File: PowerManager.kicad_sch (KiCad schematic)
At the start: 10 parts, among them U2 LM317_SOT-223

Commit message: update goose60 sch footprint
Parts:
- C10, C11, C8, C9: footprint (none) -> Capacitor_SMD:C_0201_0603Metric
- D69: footprint (none) -> Diode_SMD:D_SOD-323F
- R4, R5, R6: footprint (none) -> Resistor_SMD:R_0805_2012Metric
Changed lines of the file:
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@@
       (effects (font (size 1.27 1.27)) (justify left))
     )
-    (property "Footprint" "" (id 2) (at 158.75 116.84 0)
+    (property "Footprint" "Resistor_SMD:R_0805_2012Metric" (id 2) (at 158.75 116.84 0)
       (effects (font (size 1.27 1.27)) hide)
     )
@@
       (effects (font (size 1.27 1.27)) (justify left))
     )
-    (property "Footprint" "" (id 2) (at 129.54 123.19 0)
+    (property "Footprint" "Capacitor_SMD:C_0201_0603Metric" (id 2) (at 129.54 123.19 0)
       (effects (font (size 1.27 1.27)) hide)
     )
@@
       (effects (font (size 1.27 1.27)) (justify left))
     )
-    (property "Footprint" "" (id 2) (at 111.76 123.19 0)
+    (property "Footprint" "Diode_SMD:D_SOD-323F" (id 2) (at 111.76 123.19 0)
       (effects (font (size 1.27 1.27)) hide)
     )
@@
       (effects (font (size 1.27 1.27)) (justify left))
     )
-    (property "Footprint" "" (id 2) (at 204.47 121.92 0)
+    (property "Footprint" "Capacitor_SMD:C_0201_0603Metric" (id 2) (at 204.47 121.92 0)
       (effects (font (size 1.27 1.27)) hide)
     )
@@
       (effects (font (size 1.27 1.27)) (justify left))
     )
-    (property "Footprint" "" (id 2) (at 173.99 129.54 0)
+    (property "Footprint" "Resistor_SMD:R_0805_2012Metric" (id 2) (at 173.99 129.54 0)
       (effects (font (size 1.27 1.27)) hide)
     )
@@
       (effects (font (size 1.27 1.27)) (justify left))
     )
-    (property "Footprint" "" (id 2) (at 187.96 121.92 0)
+    (property "Footprint" "Capacitor_SMD:C_0201_0603Metric" (id 2) (at 187.96 121.92 0)
       (effects (font (size 1.27 1.27)) hide)
     )
@@
       (effects (font (size 1.27 1.27)) (justify left))
     )
-    (property "Footprint" "" (id 2) (at 144.78 129.54 0)
+    (property "Footprint" "Capacitor_SMD:C_0201_0603Metric" (id 2) (at 144.78 129.54 0)
       (effects (font (size 1.27 1.27)) hide)
     )
@@
       (effects (font (size 1.27 1.27)) (justify left))
     )
-    (property "Footprint" "" (id 2) (at 158.75 129.54 0)
+    (property "Footprint" "Resistor_SMD:R_0805_2012Metric" (id 2) (at 158.75 129.54 0)
       (effects (font (size 1.27 1.27)) hide)
     )

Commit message: update components location
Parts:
- C10, C11, C8, C9: footprint Capacitor_SMD:C_0201_0603Metric -> Capacitor_SMD:C_0603_1608Metric
- D69, D70: footprint Diode_SMD:D_SOD-323F -> Diode_SMD:D_0603_1608Metric
- R4, R5, R6: footprint Resistor_SMD:R_0805_2012Metric -> Resistor_SMD:R_0603_1608Metric
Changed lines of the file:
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@@
       (effects (font (size 1.27 1.27)) (justify left))
     )
-    (property "Footprint" "Resistor_SMD:R_0805_2012Metric" (id 2) (at 158.75 116.84 0)
+    (property "Footprint" "Resistor_SMD:R_0603_1608Metric" (id 2) (at 158.75 116.84 0)
       (effects (font (size 1.27 1.27)) hide)
     )
@@
       (effects (font (size 1.27 1.27)) (justify left))
     )
-    (property "Footprint" "Capacitor_SMD:C_0201_0603Metric" (id 2) (at 129.54 123.19 0)
+    (property "Footprint" "Capacitor_SMD:C_0603_1608Metric" (id 2) (at 129.54 123.19 0)
       (effects (font (size 1.27 1.27)) hide)
     )
@@
       (effects (font (size 1.27 1.27)) (justify left))
     )
-    (property "Footprint" "Diode_SMD:D_SOD-323F" (id 2) (at 111.76 123.19 0)
+    (property "Footprint" "Diode_SMD:D_0603_1608Metric" (id 2) (at 111.76 123.19 0)
       (effects (font (size 1.27 1.27)) hide)
     )
@@
       (effects (font (size 1.27 1.27)) (justify left))
     )
-    (property "Footprint" "Capacitor_SMD:C_0201_0603Metric" (id 2) (at 204.47 121.92 0)
+    (property "Footprint" "Capacitor_SMD:C_0603_1608Metric" (id 2) (at 204.47 121.92 0)
       (effects (font (size 1.27 1.27)) hide)
     )
@@
       (effects (font (size 1.27 1.27)) (justify left))
     )
-    (property "Footprint" "Resistor_SMD:R_0805_2012Metric" (id 2) (at 173.99 129.54 0)
+    (property "Footprint" "Resistor_SMD:R_0603_1608Metric" (id 2) (at 173.99 129.54 0)
       (effects (font (size 1.27 1.27)) hide)
     )
@@
       (effects (font (size 1.27 1.27)) (justify left))
     )
-    (property "Footprint" "Capacitor_SMD:C_0201_0603Metric" (id 2) (at 187.96 121.92 0)
+    (property "Footprint" "Capacitor_SMD:C_0603_1608Metric" (id 2) (at 187.96 121.92 0)
       (effects (font (size 1.27 1.27)) hide)
     )
@@
       (effects (font (size 1.27 1.27)) (justify left))
     )
-    (property "Footprint" "Diode_SMD:D_SOD-323F" (id 2) (at 169.545 116.84 0)
+    (property "Footprint" "Diode_SMD:D_0603_1608Metric" (id 2) (at 169.545 116.84 0)
       (effects (font (size 1.27 1.27)) hide)
     )
@@
       (effects (font (size 1.27 1.27)) (justify left))
     )
-    (property "Footprint" "Capacitor_SMD:C_0201_0603Metric" (id 2) (at 144.78 129.54 0)
+    (property "Footprint" "Capacitor_SMD:C_0603_1608Metric" (id 2) (at 144.78 129.54 0)
       (effects (font (size 1.27 1.27)) hide)
     )
@@
       (effects (font (size 1.27 1.27)) (justify left))
     )
-    (property "Footprint" "Resistor_SMD:R_0805_2012Metric" (id 2) (at 158.75 129.54 0)
+    (property "Footprint" "Resistor_SMD:R_0603_1608Metric" (id 2) (at 158.75 129.54 0)
       (effects (font (size 1.27 1.27)) hide)
     )

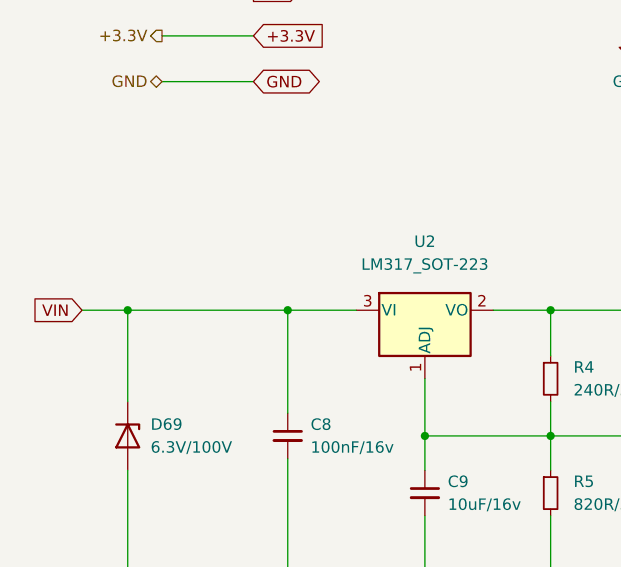
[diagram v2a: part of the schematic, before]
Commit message: add res and fix rule check fail problom
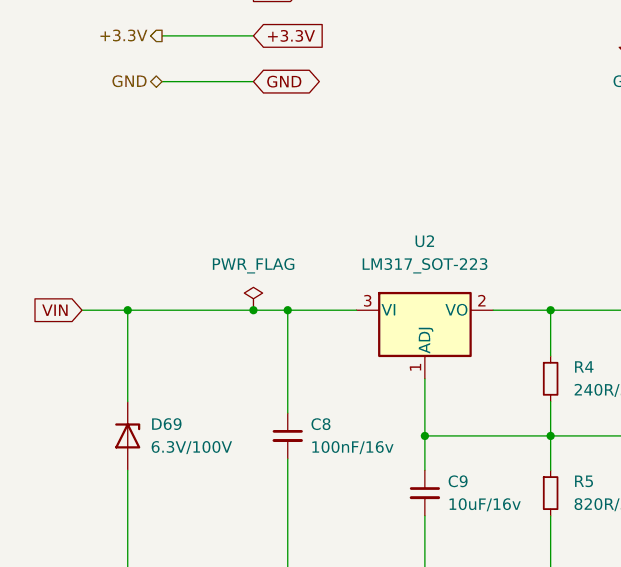
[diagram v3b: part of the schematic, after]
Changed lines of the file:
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@@
   (junction (at 158.75 138.43) (diameter 0) (color 0 0 0 0)
   )
+  (junction (at 125.73 109.22) (diameter 0) (color 0 0 0 0)
+  )
   (junction (at 173.99 123.19) (diameter 0) (color 0 0 0 0)
   )
@@
     (stroke (width 0) (type default) (color 0 0 0 0))
   )
-  (wire (pts (xy 111.76 109.22) (xy 129.54 109.22))
+  (wire (pts (xy 111.76 109.22) (xy 125.73 109.22))
     (stroke (width 0) (type default) (color 0 0 0 0))
   )
@@
   )
   (wire (pts (xy 144.78 138.43) (xy 147.32 138.43))
+    (stroke (width 0) (type default) (color 0 0 0 0))
+  )
+  (wire (pts (xy 125.73 109.22) (xy 129.54 109.22))
     (stroke (width 0) (type default) (color 0 0 0 0))
   )
@@
       (effects (font (size 1.27 1.27)) hide)
     )
+    (pin "1")
+  )
+  (symbol (lib_id "power:PWR_FLAG") (at 125.73 109.22 0) (unit 1)
+    (in_bom yes) (on_board yes) (fields_autoplaced)
+    (property "Reference" "#FLG0101" (id 0) (at 125.73 107.315 0)
+      (effects (font (size 1.27 1.27)) hide)
+    )
+    (property "Value" "PWR_FLAG" (id 1) (at 125.73 104.14 0))
+    (property "Footprint" "" (id 2) (at 125.73 109.22 0)
+      (effects (font (size 1.27 1.27)) hide)
+    )
+    (property "Datasheet" "~" (id 3) (at 125.73 109.22 0)
+      (effects (font (size 1.27 1.27)) hide)
+    )

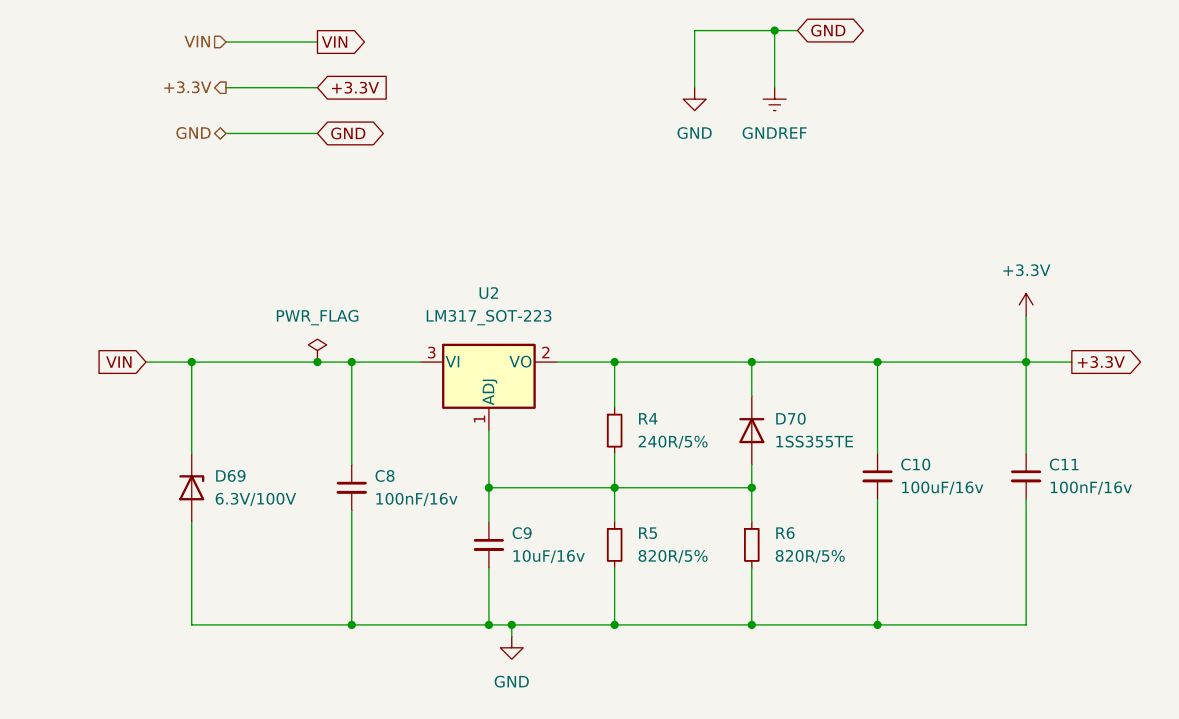
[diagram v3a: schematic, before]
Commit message: modify power/bootload circuit
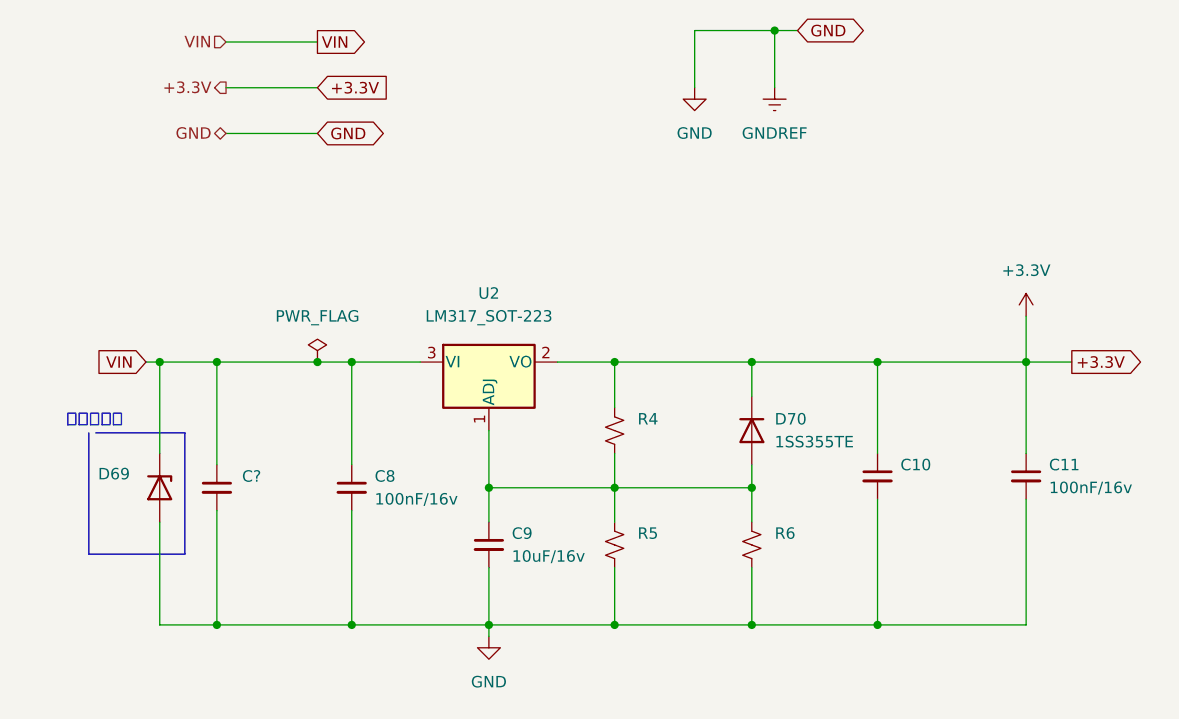
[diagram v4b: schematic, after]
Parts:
- added C?: (no value), symbol Device:C_Small
- C10: value 100uF/16v -> (none); footprint Capacitor_SMD:C_0603_1608Metric -> (none)
- D69: value 6.3V/100V -> (none)
- R4: value 240R/5% -> (none); footprint Resistor_SMD:R_0603_1608Metric -> (none); symbol Device:R_Small -> Device:R_Small_US
- R5, R6: value 820R/5% -> (none); footprint Resistor_SMD:R_0603_1608Metric -> (none); symbol Device:R_Small -> Device:R_Small_US
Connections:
- net GND: now also C?.2
- net VIN: now also C?.1
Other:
- note added: "用途待確認"
- moved on the sheet: D69

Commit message: modify pcb footprint
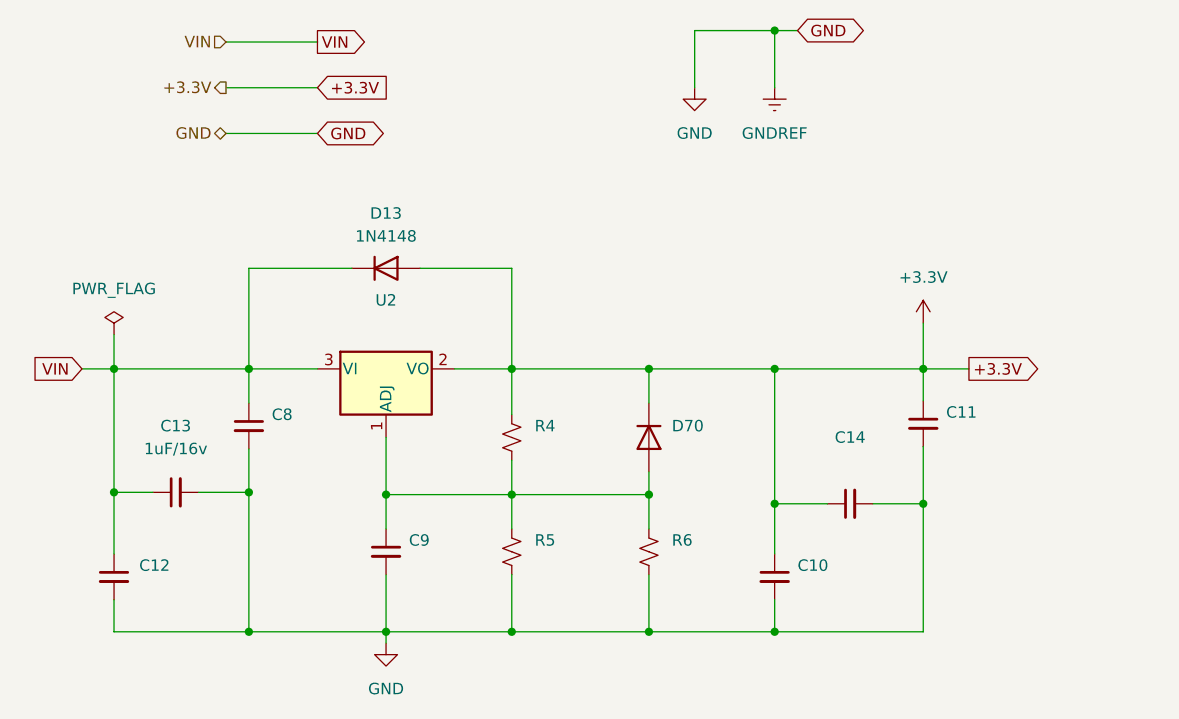
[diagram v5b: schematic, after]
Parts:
- removed D69: (no value), Diode_SMD:D_0603_1608Metric, symbol Device:D_Zener
- added C13: 1uF/16v, Capacitor_SMD:C_0603_1608Metric, symbol Device:C_Small
- added C14: (no value), Capacitor_SMD:C_0603_1608Metric, symbol Device:C_Small
- added D13: 1N4148, Diode_SMD:D_0805_2012Metric, symbol Diode:1SS355VM
- C11, C8: value 100nF/16v -> (none); footprint Capacitor_SMD:C_0603_1608Metric -> (none)
- C9: value 10uF/16v -> (none); footprint Capacitor_SMD:C_0603_1608Metric -> (none)
- D70: value 1SS355TE -> (none); footprint Diode_SMD:D_0603_1608Metric -> (none)
- U2: value LM317_SOT-223 -> (none); footprint Package_TO_SOT_SMD:SOT-223-3_TabPin2 -> (none)
- gave numbers to parts that had none: 1
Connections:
- net +3.3V: now also C14.1, D13.2 (A)
- net GND: now also C13.2, C14.2
- net VIN: now also C13.1, D13.1 (K)
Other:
- note removed: "用途待確認"
- moved on the sheet: C10, C11, C12, C8, C9, D70, R4, R5, R6, U2

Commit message: change Diode direction and update PR #1 footprint
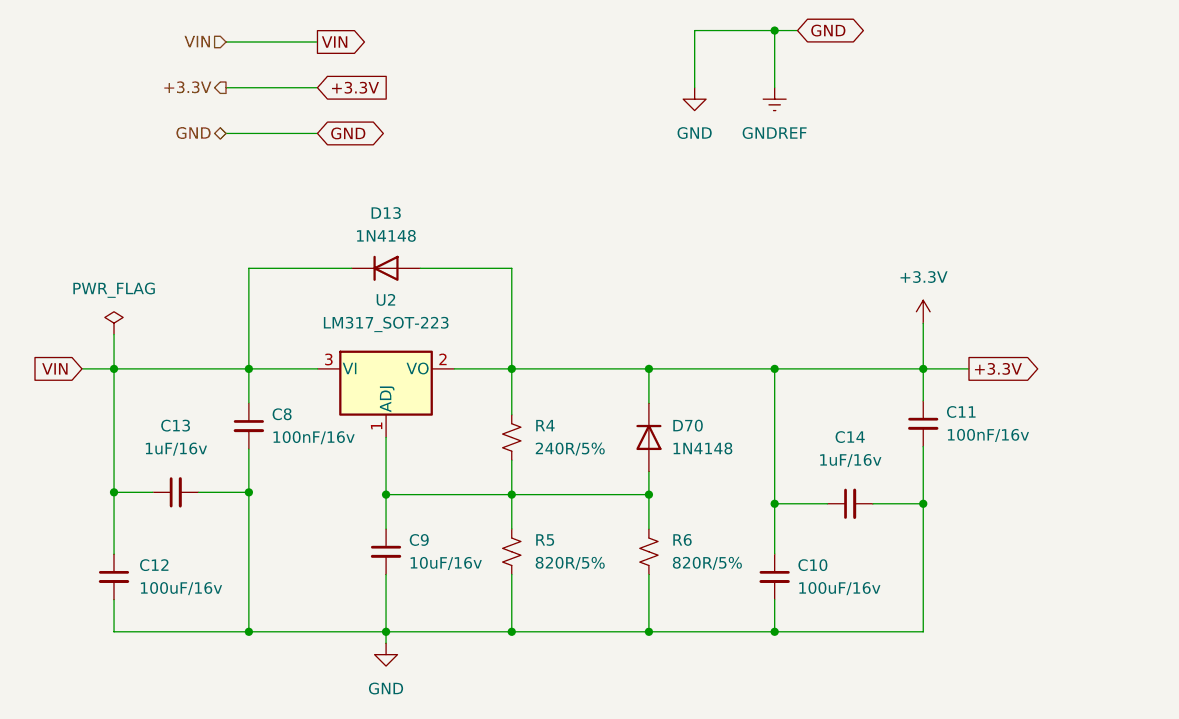
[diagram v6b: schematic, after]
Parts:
- C10, C12: value (none) -> 100uF/16v; footprint (none) -> Capacitor_SMD:C_1206_3216Metric
- C11, C8: value (none) -> 100nF/16v; footprint (none) -> Capacitor_SMD:C_0603_1608Metric
- C14: value (none) -> 1uF/16v
- C9: value (none) -> 10uF/16v; footprint (none) -> Capacitor_SMD:C_0805_2012Metric
- D70: value (none) -> 1N4148; footprint (none) -> Diode_SMD:D_0805_2012Metric
- R4: value (none) -> 240R/5%; footprint (none) -> Resistor_SMD:R_0603_1608Metric
- R5, R6: value (none) -> 820R/5%; footprint (none) -> Resistor_SMD:R_0603_1608Metric
- U2: value (none) -> LM317_SOT-223; footprint (none) -> Package_TO_SOT_SMD:SOT-223-3_TabPin2
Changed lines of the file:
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@@
       (effects (font (size 1.27 1.27)) (justify left))
     )
-    (property "Value" "" (id 1) (at 149.86 118.8719 0)
-      (effects (font (size 1.27 1.27)) (justify left))
-    )
-    (property "Footprint" "" (id 2) (at 147.32 117.602 0)
+    (property "Value" "240R/5%" (id 1) (at 149.86 118.8719 0)
+      (effects (font (size 1.27 1.27)) (justify left))
+    )
+    (property "Footprint" "Resistor_SMD:R_0603_1608Metric" (id 2) (at 147.32 117.602 0)
       (effects (font (size 1.27 1.27)) hide)
     )
@@
       (effects (font (size 1.27 1.27)) (justify left))
     )
-    (property "Value" "" (id 1) (at 120.65 117.6082 0)
-      (effects (font (size 1.27 1.27)) (justify left))
-    )
-    (property "Footprint" "" (id 2) (at 118.11 116.332 0)
+    (property "Value" "100nF/16v" (id 1) (at 120.65 117.6082 0)
+      (effects (font (size 1.27 1.27)) (justify left))
+    )
+    (property "Footprint" "Capacitor_SMD:C_0603_1608Metric" (id 2) (at 118.11 116.332 0)
       (effects (font (size 1.27 1.27)) hide)
     )
@@
       (effects (font (size 1.27 1.27)) (justify left))
     )
-    (property "Value" "" (id 1) (at 105.918 134.3722 0)
-      (effects (font (size 1.27 1.27)) (justify left))
-    )
-    (property "Footprint" "" (id 2) (at 103.124 133.096 0)
+    (property "Value" "100uF/16v" (id 1) (at 105.918 134.3722 0)
+      (effects (font (size 1.27 1.27)) (justify left))
+    )
+    (property "Footprint" "Capacitor_SMD:C_1206_3216Metric" (id 2) (at 103.124 133.096 0)
       (effects (font (size 1.27 1.27)) hide)
     )
@@
       (effects (font (size 1.27 1.27)) (justify left))
     )
-    (property "Value" "" (id 1) (at 195.58 117.3542 0)
-      (effects (font (size 1.27 1.27)) (justify left))
-    )
-    (property "Footprint" "" (id 2) (at 193.04 116.078 0)
+    (property "Value" "100nF/16v" (id 1) (at 195.58 117.3542 0)
+      (effects (font (size 1.27 1.27)) (justify left))
+    )
+    (property "Footprint" "Capacitor_SMD:C_0603_1608Metric" (id 2) (at 193.04 116.078 0)
       (effects (font (size 1.27 1.27)) hide)
     )
@@
     (in_bom yes) (on_board yes) (fields_autoplaced)
     (property "Reference" "U2" (id 0) (at 133.35 102.362 0))
-    (property "Value" "" (id 1) (at 133.35 104.902 0))
-    (property "Footprint" "" (id 2) (at 133.35 103.632 0)
+    (property "Value" "LM317_SOT-223" (id 1) (at 133.35 104.902 0))
+    (property "Footprint" "Package_TO_SOT_SMD:SOT-223-3_TabPin2" (id 2) (at 133.35 103.632 0)
       (effects (font (size 1.27 1.27) italic) hide)
     )
@@
     (in_bom yes) (on_board yes) (fields_autoplaced)
     (property "Reference" "C14" (id 0) (at 184.9183 117.602 90))
-    (property "Value" "" (id 1) (at 184.9183 120.142 90))
+    (property "Value" "1uF/16v" (id 1) (at 184.9183 120.142 90))
     (property "Footprint" "Capacitor_SMD:C_0603_1608Metric" (id 2) (at 184.912 124.968 0)
       (effects (font (size 1.27 1.27)) hide)
@@
       (effects (font (size 1.27 1.27)) (justify left))
     )
-    (property "Value" "" (id 1) (at 165.1 131.5719 0)
-      (effects (font (size 1.27 1.27)) (justify left))
-    )
-    (property "Footprint" "" (id 2) (at 162.56 130.302 0)
+    (property "Value" "820R/5%" (id 1) (at 165.1 131.5719 0)
+      (effects (font (size 1.27 1.27)) (justify left))
+    )
+    (property "Footprint" "Resistor_SMD:R_0603_1608Metric" (id 2) (at 162.56 130.302 0)
       (effects (font (size 1.27 1.27)) hide)
     )
@@
       (effects (font (size 1.27 1.27)) (justify left))
     )
-    (property "Value" "" (id 1) (at 179.07 134.3722 0)
-      (effects (font (size 1.27 1.27)) (justify left))
-    )
-    (property "Footprint" "" (id 2) (at 176.53 133.096 0)
+    (property "Value" "100uF/16v" (id 1) (at 179.07 134.3722 0)
+      (effects (font (size 1.27 1.27)) (justify left))
+    )
+    (property "Footprint" "Capacitor_SMD:C_1206_3216Metric" (id 2) (at 176.53 133.096 0)
       (effects (font (size 1.27 1.27)) hide)
     )
@@
       (effects (font (size 1.27 1.27)) (justify left))
     )
-    (property "Value" "" (id 1) (at 165.1 118.8719 90)
-      (effects (font (size 1.27 1.27)) (justify left))
-    )
-    (property "Footprint" "" (id 2) (at 158.115 117.602 0)
+    (property "Value" "1N4148" (id 1) (at 165.1 118.8719 90)
+      (effects (font (size 1.27 1.27)) (justify left))
+    )
+    (property "Footprint" "Diode_SMD:D_0805_2012Metric" (id 2) (at 158.115 117.602 0)
       (effects (font (size 1.27 1.27)) hide)
     )
@@
       (effects (font (size 1.27 1.27)) (justify left))
     )
-    (property "Value" "" (id 1) (at 135.89 131.5782 0)
-      (effects (font (size 1.27 1.27)) (justify left))
-    )
-    (property "Footprint" "" (id 2) (at 133.35 130.302 0)
+    (property "Value" "10uF/16v" (id 1) (at 135.89 131.5782 0)
+      (effects (font (size 1.27 1.27)) (justify left))
+    )
+    (property "Footprint" "Capacitor_SMD:C_0805_2012Metric" (id 2) (at 133.35 130.302 0)
       (effects (font (size 1.27 1.27)) hide)
     )
@@
       (effects (font (size 1.27 1.27)) (justify left))
     )
-    (property "Value" "" (id 1) (at 149.86 131.5719 0)
-      (effects (font (size 1.27 1.27)) (justify left))
-    )
-    (property "Footprint" "" (id 2) (at 147.32 130.302 0)
-      (effects (font (size 1.27 1.27)) hide)
-    )
+    (property "Value" "820R/5%" (id 1) (at 149.86 131.5719 0)
+      (effects (font (size 1.27 1.27)) (justify left))
+    )
+    (property "Footprint" "Resistor_SMD:R_0603_1608Metric" (id 2) (at 147.32 130.302 0)
+      (effects (font (size 1.27 1.27)) hide)
+    )
